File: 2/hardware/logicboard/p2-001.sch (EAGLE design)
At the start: 68 parts, among them IC1 74LS06N, IC101 74LS153D, IC102 LTC485S, IC103 LTC485S, IC2 4066N, J1 MKR, J101 Qwiic, J102 Qwiic, J103 Qwiic, J104 Qwiic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

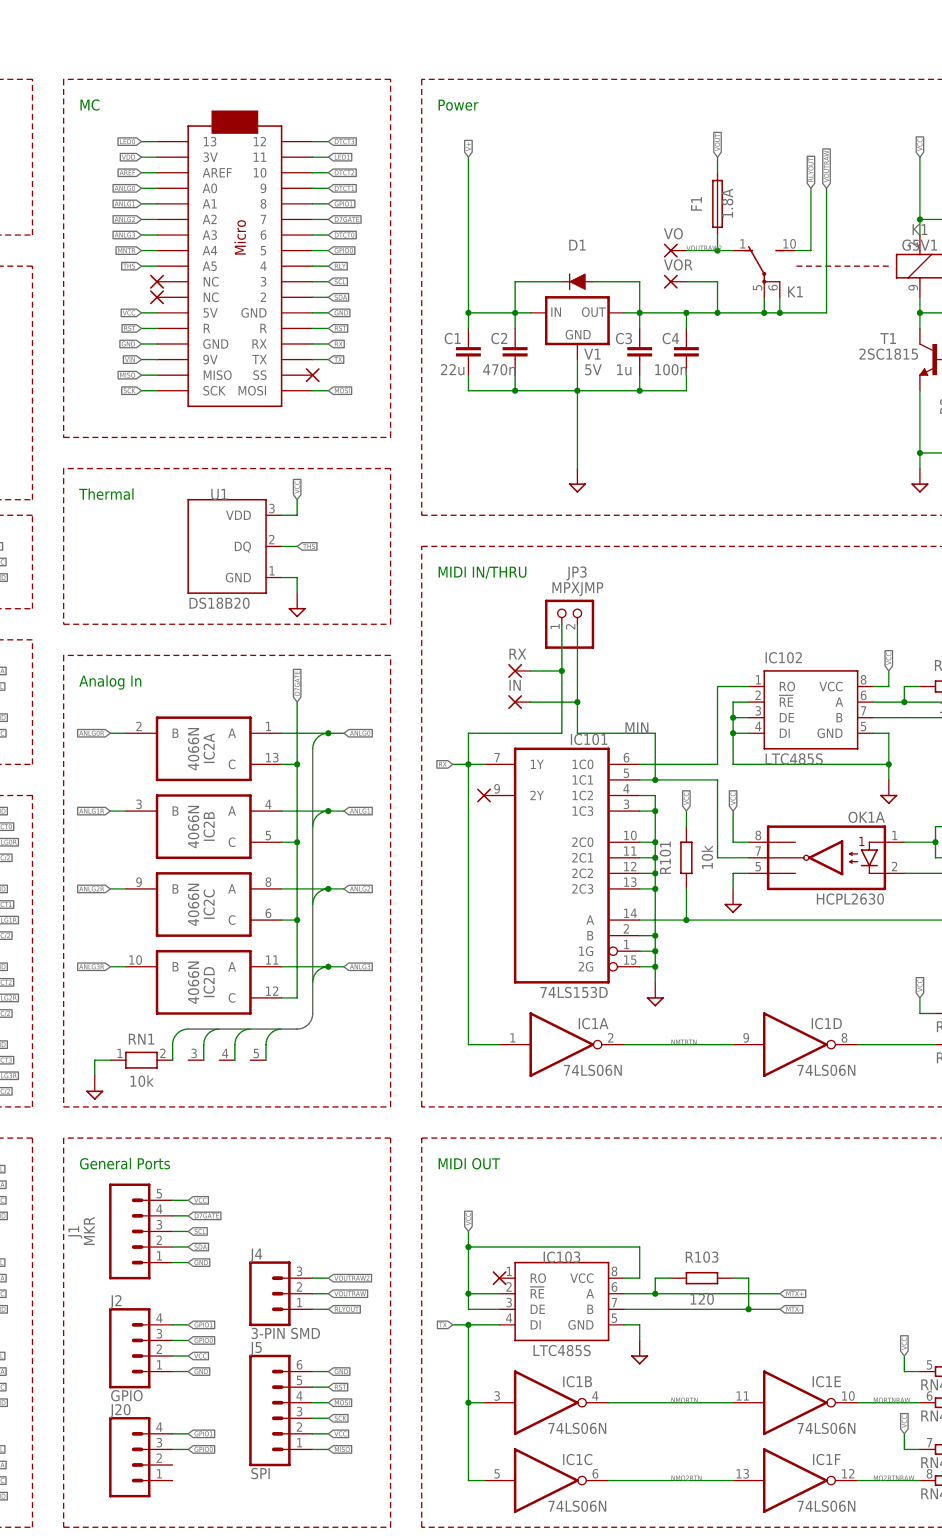
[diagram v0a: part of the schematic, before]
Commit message: Clean up of schematic.
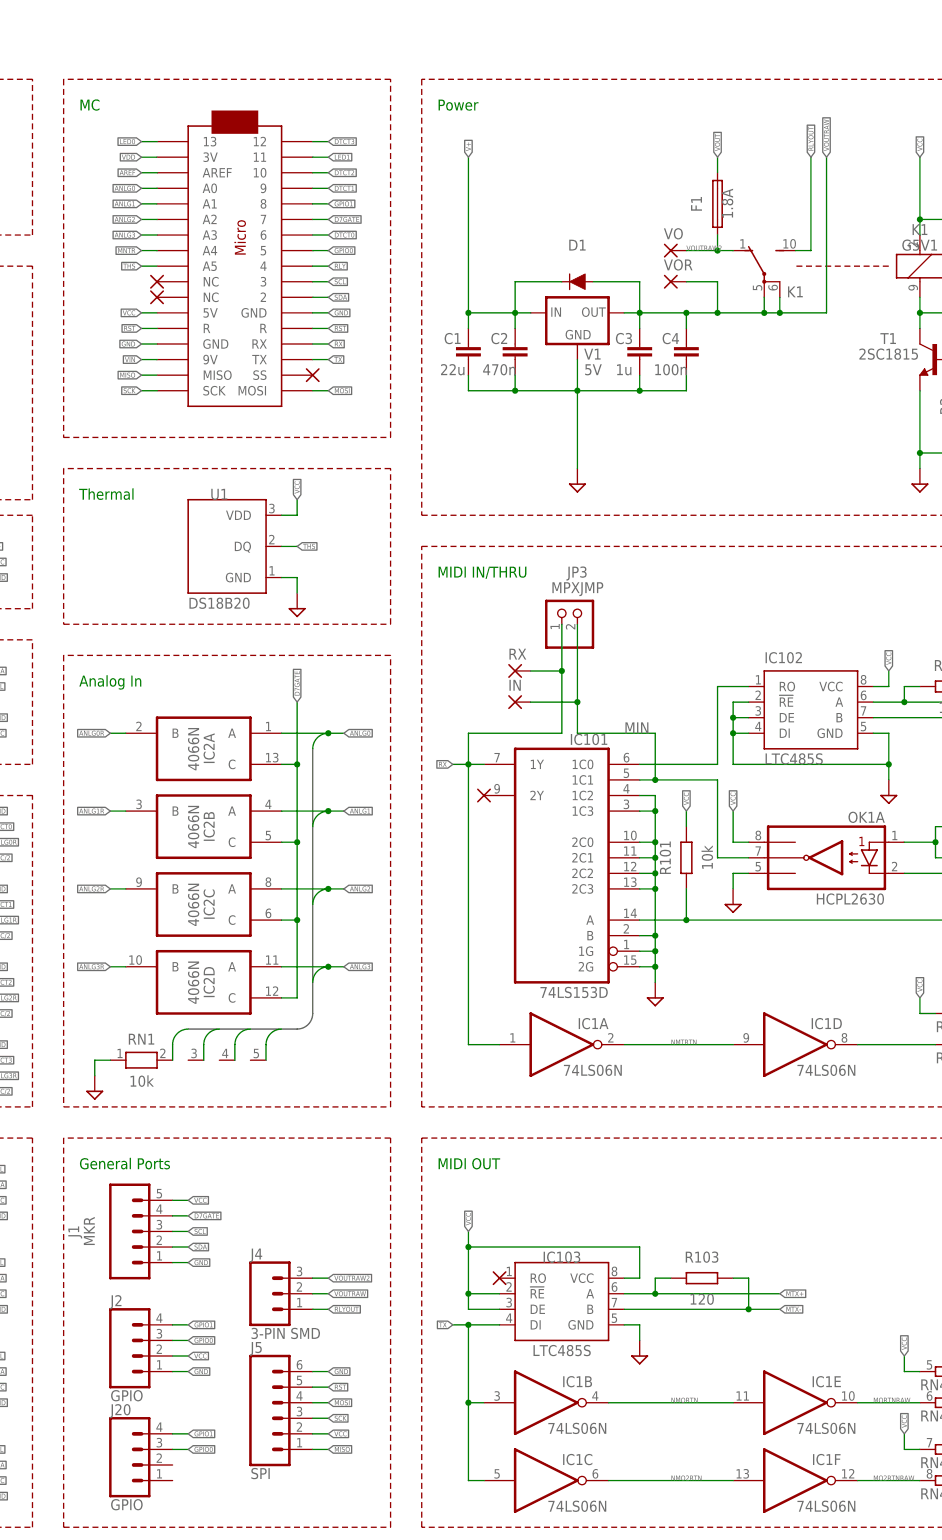
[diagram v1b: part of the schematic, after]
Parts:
- J20: value (none) -> GPIO
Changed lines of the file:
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@@
 <setting verticaltext="up"/>
 </settings>
-<grid distance="0.1" unitdist="inch" unit="inch" style="lines" multiple="1" display="no" altdistance="0.01" altunitdist="inch" altunit="inch"/>
+<grid distance="0.1" unitdist="inch" unit="inch" style="lines" multiple="1" display="yes" altdistance="0.01" altunitdist="inch" altunit="inch"/>
 <layers>
 <layer number="1" name="Top" color="4" fill="1" visible="no" active="no"/>
@@
 <part name="J5" library="SparkFun-Connectors" library_urn="urn:adsk.eagle:library:513" deviceset="CONN_06" device="1.27MM" package3d_urn="urn:adsk.eagle:package:38131/1" value="SPI"/>
 <part name="J2" library="SparkFun-Connectors" library_urn="urn:adsk.eagle:library:513" deviceset="CONN_04" device="JST-PTH" package3d_urn="urn:adsk.eagle:package:38101/1" value="GPIO"/>
-<part name="J20" library="SparkFun-Connectors" library_urn="urn:adsk.eagle:library:513" deviceset="CONN_04" device="1.27MM" package3d_urn="urn:adsk.eagle:package:38086/1"/>
+<part name="J20" library="SparkFun-Connectors" library_urn="urn:adsk.eagle:library:513" deviceset="CONN_04" device="1.27MM" package3d_urn="urn:adsk.eagle:package:38086/1" value="GPIO"/>
 </parts>
 <sheets>
@@
 <wire x1="172.72" y1="205.74" x2="180.34" y2="205.74" width="0.1524" layer="91"/>
 <junction x="172.72" y="205.74"/>
-<wire x1="180.34" y1="205.74" x2="180.34" y2="226.06" width="0.1524" layer="91"/>
-<label x="180.34" y="226.06" size="0.8128" layer="95" rot="R90" xref="yes"/>
+<wire x1="180.34" y1="205.74" x2="180.34" y2="231.14" width="0.1524" layer="91"/>
+<label x="180.34" y="231.14" size="0.8128" layer="95" rot="R90" xref="yes"/>
 <pinref part="VOR" gate="1" pin="P"/>
 </segment>
@@
 <pinref part="K1" gate="2" pin="S"/>
 <wire x1="175.26" y1="215.9" x2="177.8" y2="215.9" width="0.1524" layer="91"/>
-<wire x1="177.8" y1="215.9" x2="177.8" y2="226.06" width="0.1524" layer="91"/>
-<label x="177.8" y="226.06" size="0.8128" layer="95" rot="R90" xref="yes"/>
-</segment>
-<segment>
+<wire x1="177.8" y1="215.9" x2="177.8" y2="231.14" width="0.1524" layer="91"/>
+<label x="177.8" y="231.14" size="0.8128" layer="95" rot="R90" xref="yes"/>
+</segment>
+<segment>

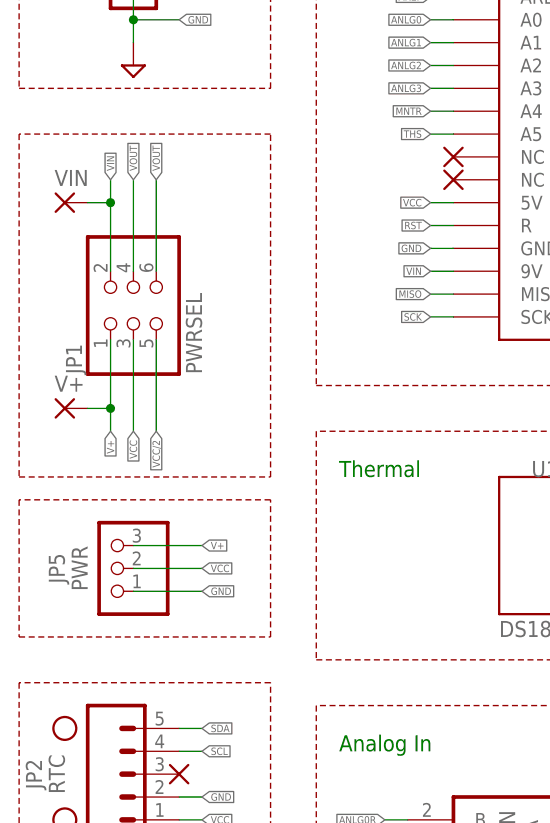
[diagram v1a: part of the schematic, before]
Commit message: Trying to add 4-pin front con.
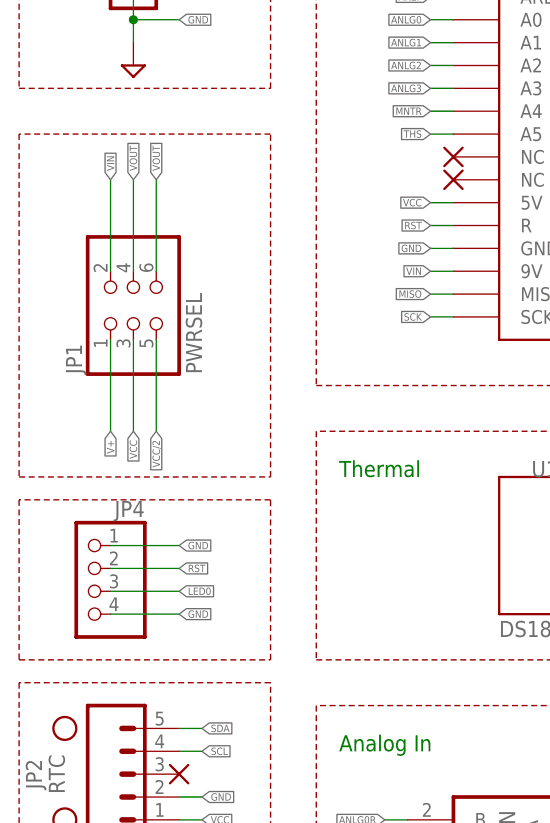
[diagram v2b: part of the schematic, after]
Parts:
- removed JP5: PWR, pinhead:PINHD-1X3
- removed V+, VIN: (no value), wirepad:SMD2
- added JP4: (no value), pinhead:PINHD-1X4
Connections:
- net GND: now also JP4.1, JP4.4; no longer JP5.1
- net LED0: now also JP4.3
- net RST: now also JP4.2
- net V+: no longer JP5.3, V+.P
- net VCC: no longer JP5.2
- net VIN: no longer VIN.P
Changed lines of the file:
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@@
 <setting verticaltext="up"/>
 </settings>
-<grid distance="0.1" unitdist="inch" unit="inch" style="lines" multiple="1" display="yes" altdistance="0.01" altunitdist="inch" altunit="inch"/>
+<grid distance="0.1" unitdist="inch" unit="inch" style="lines" multiple="1" display="no" altdistance="0.01" altunitdist="inch" altunit="inch"/>
 <layers>
 <layer number="1" name="Top" color="4" fill="1" visible="no" active="no"/>
@@
 <part name="XJP2_3" library="wirepad" library_urn="urn:adsk.eagle:library:412" deviceset="PAD-N" device=""/>
 <part name="JP1" library="pinhead" library_urn="urn:adsk.eagle:library:325" deviceset="PINHD-2X3" device="" package3d_urn="urn:adsk.eagle:package:22462/2" value="PWRSEL"/>
-<part name="JP5" library="pinhead" library_urn="urn:adsk.eagle:library:325" deviceset="PINHD-1X3" device="" package3d_urn="urn:adsk.eagle:package:22458/2" value="PWR"/>
 <part name="RX" library="wirepad" library_urn="urn:adsk.eagle:library:412" deviceset="SMD2" device="" package3d_urn="urn:adsk.eagle:package:30839/1"/>
 <part name="IN" library="wirepad" library_urn="urn:adsk.eagle:library:412" deviceset="SMD2" device="" package3d_urn="urn:adsk.eagle:package:30839/1"/>
@@
 <part name="OK1" library="optocoupler" library_urn="urn:adsk.eagle:library:320" deviceset="HCPL2630" device="" package3d_urn="urn:adsk.eagle:package:21941/1"/>
 <part name="SUPPLY1" library="supply2" deviceset="GND" device=""/>
-<part name="V+" library="wirepad" library_urn="urn:adsk.eagle:library:412" deviceset="SMD2" device="" package3d_urn="urn:adsk.eagle:package:30839/1"/>
-<part name="VIN" library="wirepad" library_urn="urn:adsk.eagle:library:412" deviceset="SMD2" device="" package3d_urn="urn:adsk.eagle:package:30839/1"/>
 <part name="SUPPLY6" library="supply2" deviceset="GND" device=""/>
 <part name="VO" library="wirepad" library_urn="urn:adsk.eagle:library:412" deviceset="SMD2" device="" package3d_urn="urn:adsk.eagle:package:30839/1"/>
@@
 <part name="J2" library="SparkFun-Connectors" library_urn="urn:adsk.eagle:library:513" deviceset="CONN_04" device="JST-PTH" package3d_urn="urn:adsk.eagle:package:38101/1" value="GPIO"/>
 <part name="J20" library="SparkFun-Connectors" library_urn="urn:adsk.eagle:library:513" deviceset="CONN_04" device="1.27MM" package3d_urn="urn:adsk.eagle:package:38086/1" value="GPIO"/>
+<part name="JP4" library="pinhead" library_urn="urn:adsk.eagle:library:325" deviceset="PINHD-1X4" device="" package3d_urn="urn:adsk.eagle:package:22407/2"/>
 </parts>
 <sheets>
@@
 <wire x1="50.8" y1="152.4" x2="22.86" y2="152.4" width="0.1524" layer="94" style="shortdash"/>
 <wire x1="22.86" y1="152.4" x2="22.86" y2="132.08" width="0.1524" layer="94" style="shortdash"/>
-<wire x1="22.86" y1="157.48" x2="50.8" y2="157.48" width="0.1524" layer="94" style="shortdash"/>
-<wire x1="50.8" y1="157.48" x2="50.8" y2="172.72" width="0.1524" layer="94" style="shortdash"/>
+<wire x1="22.86" y1="154.94" x2="50.8" y2="154.94" width="0.1524" layer="94" style="shortdash"/>
+<wire x1="50.8" y1="154.94" x2="50.8" y2="172.72" width="0.1524" layer="94" style="shortdash"/>
 <wire x1="50.8" y1="172.72" x2="22.86" y2="172.72" width="0.1524" layer="94" style="shortdash"/>
-<wire x1="22.86" y1="172.72" x2="22.86" y2="157.48" width="0.1524" layer="94" style="shortdash"/>
+<wire x1="22.86" y1="172.72" x2="22.86" y2="154.94" width="0.1524" layer="94" style="shortdash"/>
 <wire x1="22.86" y1="175.26" x2="50.8" y2="175.26" width="0.1524" layer="94" style="shortdash"/>
 <wire x1="50.8" y1="175.26" x2="50.8" y2="213.36" width="0.1524" layer="94" style="shortdash"/>
@@
 <attribute name="VALUE" x="43.18" y="186.69" size="1.778" layer="96" rot="R90"/>
 </instance>
-<instance part="JP5" gate="A" x="33.02" y="165.1" smashed="yes" rot="R180">
-<attribute name="NAME" x="27.94" y="165.1" size="1.778" layer="95" rot="R90" align="bottom-center"/>
-<attribute name="VALUE" x="30.48" y="165.1" size="1.778" layer="96" rot="R90" align="bottom-center"/>
-</instance>
 <instance part="RX" gate="1" x="129.54" y="147.32" smashed="yes">
 <attribute name="NAME" x="128.397" y="149.1742" size="1.778" layer="95"/>
@@
 </instance>
 <instance part="SUPPLY1" gate="GND" x="236.22" y="35.56" smashed="yes"/>
-<instance part="V+" gate="1" x="27.94" y="182.88" smashed="yes">
-<attribute name="NAME" x="26.797" y="184.7342" size="1.778" layer="95"/>
-<attribute name="VALUE" x="26.797" y="179.578" size="1.778" layer="96"/>
-</instance>
-<instance part="VIN" gate="1" x="27.94" y="205.74" smashed="yes">
-<attribute name="NAME" x="26.797" y="207.5942" size="1.778" layer="95"/>
-<attribute name="VALUE" x="26.797" y="202.438" size="1.778" layer="96"/>
-</instance>
 <instance part="SUPPLY6" gate="GND" x="259.08" y="83.82" smashed="yes"/>
 <instance part="VO" gate="1" x="154.94" y="215.9" smashed="yes">
@@
 <attribute name="VALUE" x="63.5" y="10.414" size="1.778" layer="96" font="vector"/>
 <attribute name="NAME" x="63.5" y="25.908" size="1.778" layer="95" font="vector"/>
+</instance>
+<instance part="JP4" gate="A" x="30.48" y="162.56" smashed="yes" rot="MR0">
+<attribute name="NAME" x="36.83" y="170.815" size="1.778" layer="95" rot="MR0"/>
+<attribute name="VALUE" x="36.83" y="154.94" size="1.778" layer="96" rot="MR0"/>
 </instance>
 </instances>
@@
 </segment>
 <segment>
-<pinref part="JP5" gate="A" pin="1"/>
-<wire x1="35.56" y1="162.56" x2="43.18" y2="162.56" width="0.1524" layer="91"/>
-<label x="43.18" y="162.56" size="0.8128" layer="95" xref="yes"/>
-</segment>
-<segment>
 <pinref part="OK1" gate="B" pin="C2"/>
 <wire x1="238.76" y1="43.18" x2="236.22" y2="43.18" width="0.1524" layer="91"/>
@@
 <label x="76.2" y="33.02" size="0.8128" layer="95" xref="yes"/>
 <pinref part="J2" gate="G$1" pin="1"/>
+</segment>
+<segment>
+<pinref part="JP4" gate="A" pin="1"/>
+<wire x1="33.02" y1="167.64" x2="40.64" y2="167.64" width="0.1524" layer="91"/>
+<label x="40.64" y="167.64" size="0.8128" layer="95" xref="yes"/>
+</segment>
+<segment>
+<pinref part="JP4" gate="A" pin="4"/>
+<wire x1="33.02" y1="160.02" x2="40.64" y2="160.02" width="0.1524" layer="91"/>
+<label x="40.64" y="160.02" size="0.8128" layer="95" xref="yes"/>
 </segment>
 </net>
@@
 </segment>
 <segment>
-<pinref part="JP5" gate="A" pin="2"/>
-<wire x1="35.56" y1="165.1" x2="43.18" y2="165.1" width="0.1524" layer="91"/>
-<label x="43.18" y="165.1" size="0.8128" layer="95" xref="yes"/>
-</segment>
-<segment>
 <pinref part="RN3" gate="1" pin="1"/>
 <wire x1="238.76" y1="157.48" x2="238.76" y2="160.02" width="0.1524" layer="91"/>
@@
 <label x="99.06" y="30.48" size="0.8128" layer="95" xref="yes"/>
 <pinref part="J5" gate="G$1" pin="5"/>
+</segment>
+<segment>
+<pinref part="JP4" gate="A" pin="2"/>
+<wire x1="33.02" y1="165.1" x2="40.64" y2="165.1" width="0.1524" layer="91"/>
+<label x="40.64" y="165.1" size="0.8128" layer="95" xref="yes"/>
 </segment>
 </net>
@@
 <label x="314.96" y="134.62" size="0.8128" layer="95" rot="R180" xref="yes"/>
 </segment>
+<segment>
+<pinref part="JP4" gate="A" pin="3"/>
+<wire x1="33.02" y1="162.56" x2="40.64" y2="162.56" width="0.1524" layer="91"/>
+<label x="40.64" y="162.56" size="0.8128" layer="95" xref="yes"/>
+</segment>
 </net>
 <net name="VDD" class="2">
@@
 <segment>
 <pinref part="JP1" gate="A" pin="2"/>
-<wire x1="33.02" y1="198.12" x2="33.02" y2="205.74" width="0.1524" layer="91"/>
+<wire x1="33.02" y1="198.12" x2="33.02" y2="208.28" width="0.1524" layer="91"/>
 <label x="33.02" y="208.28" size="0.8128" layer="95" rot="R90" xref="yes"/>
-<wire x1="33.02" y1="205.74" x2="33.02" y2="208.28" width="0.1524" layer="91"/>
-<wire x1="33.02" y1="205.74" x2="30.48" y2="205.74" width="0.1524" layer="91"/>
-<junction x="33.02" y="205.74"/>
-<pinref part="VIN" gate="1" pin="P"/>
 </segment>
 </net>
@@
 <segment>
 <pinref part="JP1" gate="A" pin="1"/>
-<wire x1="33.02" y1="190.5" x2="33.02" y2="182.88" width="0.1524" layer="91"/>
+<wire x1="33.02" y1="190.5" x2="33.02" y2="180.34" width="0.1524" layer="91"/>
 <label x="33.02" y="180.34" size="0.8128" layer="95" rot="R270" xref="yes"/>
-<wire x1="33.02" y1="182.88" x2="33.02" y2="180.34" width="0.1524" layer="91"/>
-<wire x1="33.02" y1="182.88" x2="30.48" y2="182.88" width="0.1524" layer="91"/>
-<junction x="33.02" y="182.88"/>
-<pinref part="V+" gate="1" pin="P"/>
-</segment>
-<segment>
-<pinref part="JP5" gate="A" pin="3"/>
-<wire x1="35.56" y1="167.64" x2="43.18" y2="167.64" width="0.1524" layer="91"/>
-<label x="43.18" y="167.64" size="0.8128" layer="95" xref="yes"/>
-</segment>
-<segment>
+</segment>
+<segment>

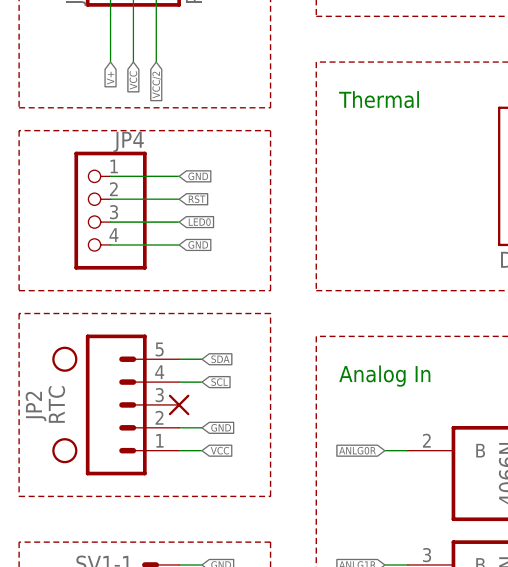
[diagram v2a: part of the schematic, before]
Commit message: LEDSW connector (temporarily named JP4) is added.
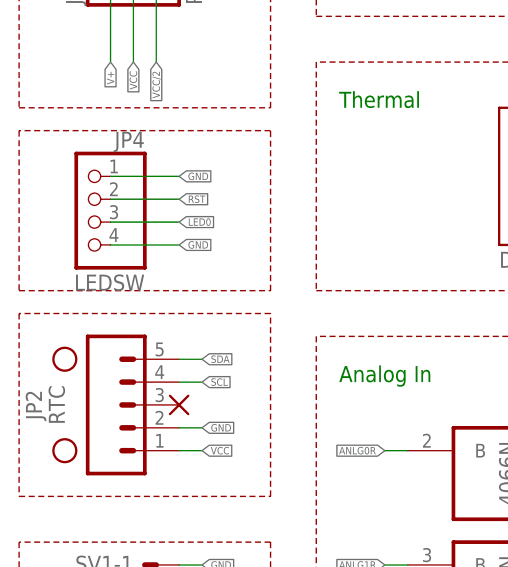
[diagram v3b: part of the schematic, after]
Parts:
- JP4: value (none) -> LEDSW
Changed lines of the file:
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@@
 <part name="J2" library="SparkFun-Connectors" library_urn="urn:adsk.eagle:library:513" deviceset="CONN_04" device="JST-PTH" package3d_urn="urn:adsk.eagle:package:38101/1" value="GPIO"/>
 <part name="J20" library="SparkFun-Connectors" library_urn="urn:adsk.eagle:library:513" deviceset="CONN_04" device="1.27MM" package3d_urn="urn:adsk.eagle:package:38086/1" value="GPIO"/>
-<part name="JP4" library="pinhead" library_urn="urn:adsk.eagle:library:325" deviceset="PINHD-1X4" device="" package3d_urn="urn:adsk.eagle:package:22407/2"/>
+<part name="JP4" library="pinhead" library_urn="urn:adsk.eagle:library:325" deviceset="PINHD-1X4" device="" package3d_urn="urn:adsk.eagle:package:22407/2" value="LEDSW"/>
 </parts>
 <sheets>
